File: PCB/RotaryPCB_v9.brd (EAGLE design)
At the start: 114.5 x 67.5 mm, 4 parts

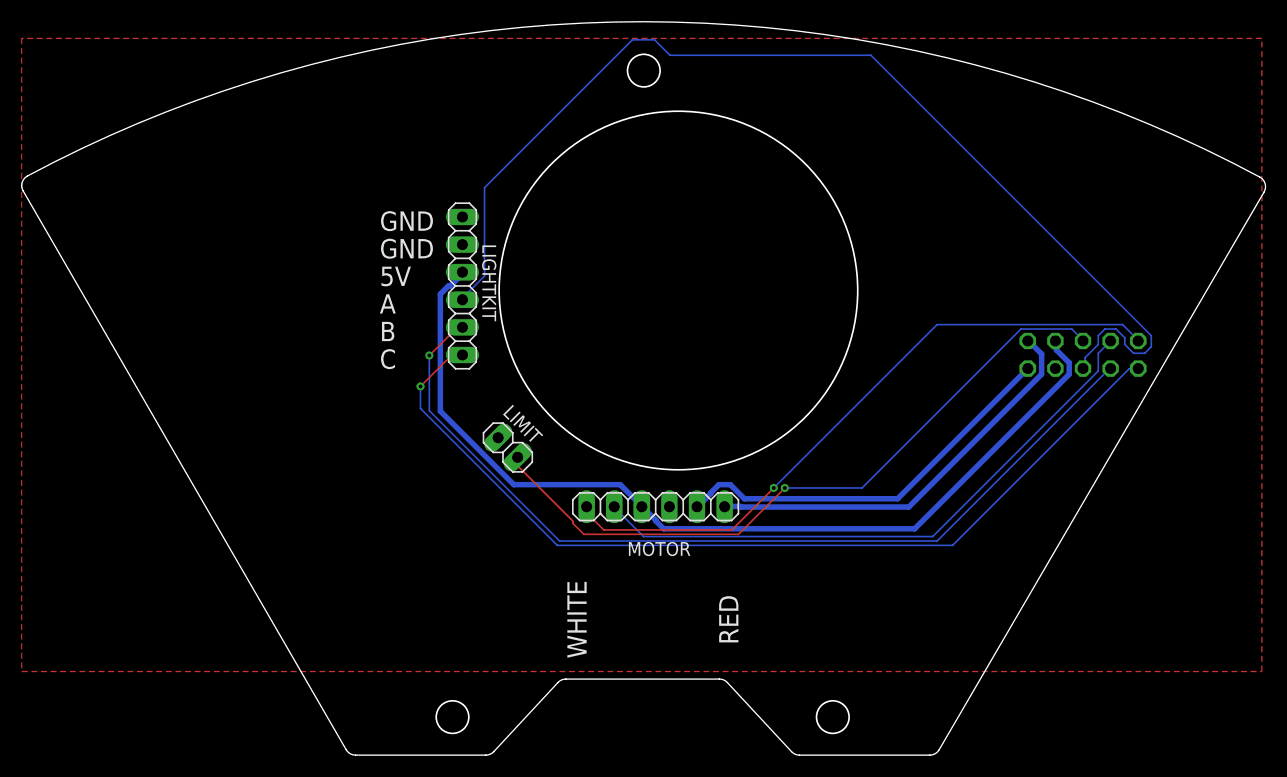
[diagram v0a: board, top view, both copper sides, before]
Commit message: This version uses thicker traces and adds a copper pour. The lifter board is a four layer board. The order of the connection pins on the rotary has changed. Do NOT use the same cable as the older board. The order was changed to allow using a silicone ribbon cable.
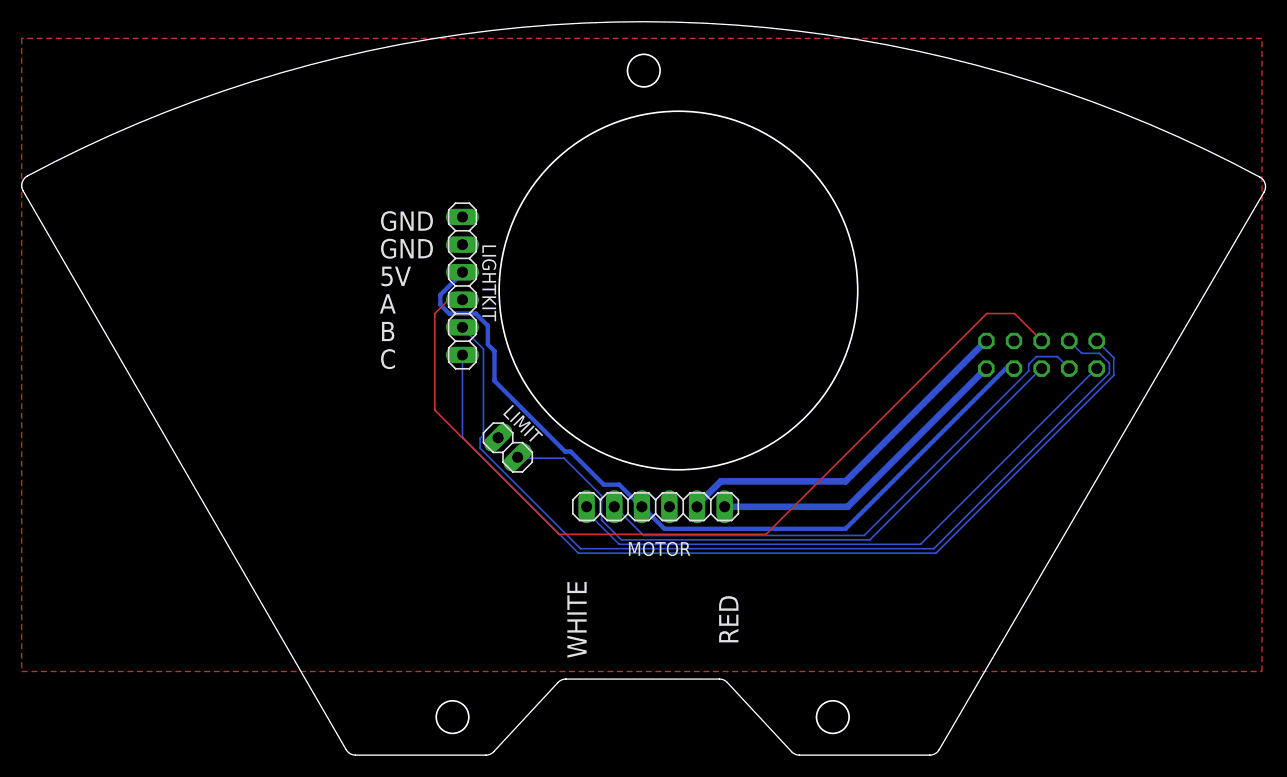
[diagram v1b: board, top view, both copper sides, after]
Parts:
- moved INPUT 3.81 mm to (93.9, 41.9)
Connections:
- net +5V: now also INPUT.7; no longer INPUT.8
- net GND: now also INPUT.8; no longer INPUT.7
- net LKIT_A: now also INPUT.6; no longer INPUT.5
- net LKIT_B: now also INPUT.4; no longer INPUT.3
- net LKIT_C: now also INPUT.2; no longer INPUT.1
- net RMOT1: now also INPUT.10; no longer INPUT.9
- net RMOT2: now also INPUT.9; no longer INPUT.10
- net RTR_ENA: now also INPUT.3; no longer INPUT.4
- net RTR_ENB: now also INPUT.1; no longer INPUT.2
- net RTR_LIMIT: now also INPUT.5; no longer INPUT.6
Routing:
- net LKIT_A: track 100.7 -> 82.0 mm
- net +5V: track 85.6 -> 73.9 mm
- net RMOT2: track 37.9 -> 29.4 mm
- net RTR_ENB: track 60.5 -> 55.4 mm, vias 1 -> 0
- net RTR_ENA: track 55.3 -> 50.6 mm
- net RTR_LIMIT: track 63.9 -> 59.3 mm, vias 1 -> 0
- net RMOT1: track 36.8 -> 33.1 mm
- net LKIT_C: track 85.1 -> 82.5 mm, vias 1 -> 0
- net LKIT_B: track 83.5 -> 85.9 mm, vias 1 -> 0
